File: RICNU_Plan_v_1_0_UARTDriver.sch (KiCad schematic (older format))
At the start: 7 parts, among them SW1 CL-SB-12B-01T, U3 SN74AHC126

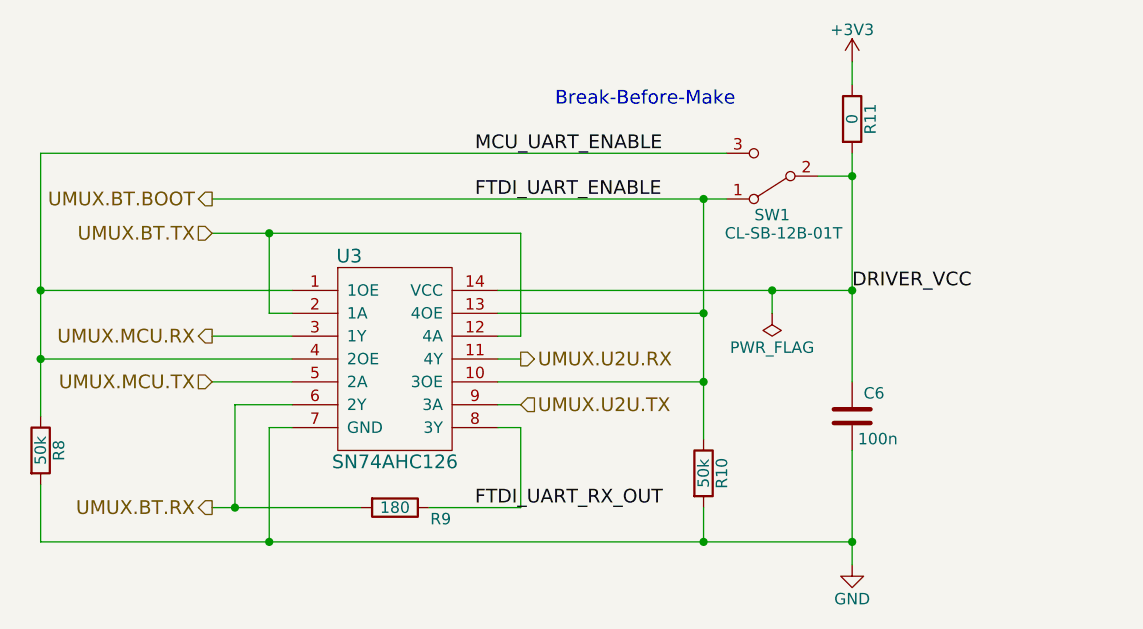
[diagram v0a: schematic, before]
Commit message: Re-routed CAN, RS-485, and debug connectors (wrong polarity in all)
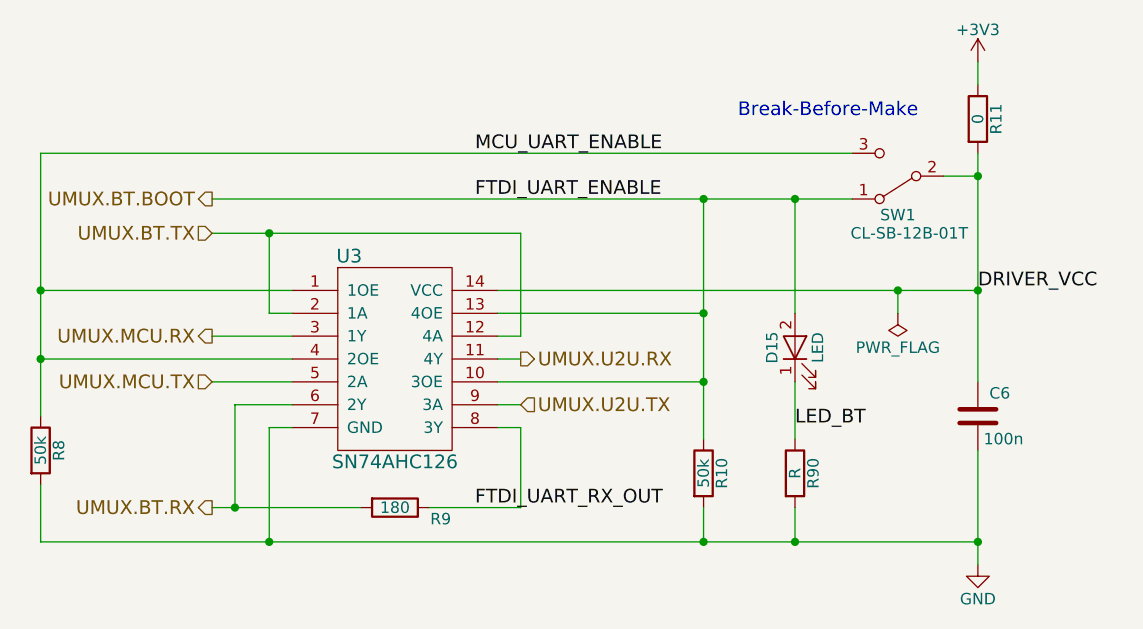
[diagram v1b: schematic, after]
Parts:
- added D15: LED, LEDs:LED_0402, symbol LED
- added R90: R, Resistors_SMD:R_0402_NoSilk, symbol R
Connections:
- net GND: now also R90.2
- net UMUX.BT.BOOT: now also D15.2 (A)
- new net LED_BT: D15.1 (K), R90.1
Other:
- moved on the sheet: C6, R11, SW1
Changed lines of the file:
@@
 L SW_SPDT SW1
 U 1 1 59E13A51
-P 7200 3300
-F 0 "SW1" H 7200 3470 50  0000 C CNN
-F 1 "CL-SB-12B-01T" H 7150 3550 50  0000 C CNN
-F 2 "RICNU_Plan_v_1_0:CL-SB-12B-01T" H 7200 3300 50  0001 C CNN
-F 3 "" H 7200 3300 50  0001 C CNN
-	1    7200 3300
+P 7750 3300
+F 0 "SW1" H 7750 3470 50  0000 C CNN
+F 1 "CL-SB-12B-01T" H 7700 3550 50  0000 C CNN
+F 2 "RICNU_Plan_v_1_0:CL-SB-12B-01T" H 7750 3300 50  0001 C CNN
+F 3 "" H 7750 3300 50  0001 C CNN
+	1    7750 3300
 	-1   0    0    1
 $EndComp
@@
 	6000 4000 6100 4000
 Wire Wire Line
-	6100 4000 6100 3550
-Wire Wire Line
-	6100 3550 4750 3550
+	6100 3550 6100 4000
+Wire Wire Line
+	4750 3550 6100 3550
 Wire Wire Line
 	4850 4750 4850 4300
@@
 Connection ~ 4000 3800
 Wire Wire Line
-	4750 3400 7000 3400
+	4750 3400 7550 3400
 Wire Wire Line
 	6900 3400 6900 4450
@@
 Connection ~ 4000 4100
 Wire Wire Line
-	4000 3200 7000 3200
+	4000 3200 7550 3200
 Connection ~ 6900 4200
 Connection ~ 6900 3900
@@
 L GND #PWR020
 U 1 1 59E69F5D
-P 7550 5000
-F 0 "#PWR020" H 7550 4750 50  0001 C CNN
-F 1 "GND" H 7550 4850 50  0000 C CNN
-F 2 "" H 7550 5000 50  0001 C CNN
-F 3 "" H 7550 5000 50  0001 C CNN
-	1    7550 5000
+P 8100 5000
+F 0 "#PWR020" H 8100 4750 50  0001 C CNN
+F 1 "GND" H 8100 4850 50  0000 C CNN
+F 2 "" H 8100 5000 50  0001 C CNN
+F 3 "" H 8100 5000 50  0001 C CNN
+	1    8100 5000
 	1    0    0    -1
 $EndComp
@@
 L +3V3 #PWR021
 U 1 1 59FDD411
-P 7550 2800
-F 0 "#PWR021" H 7550 2650 50  0001 C CNN
-F 1 "+3V3" H 7550 2940 50  0000 C CNN
-F 2 "" H 7550 2800 50  0001 C CNN
-F 3 "" H 7550 2800 50  0001 C CNN
-	1    7550 2800
+P 8100 2800
+F 0 "#PWR021" H 8100 2650 50  0001 C CNN
+F 1 "+3V3" H 8100 2940 50  0000 C CNN
+F 2 "" H 8100 2800 50  0001 C CNN
+F 3 "" H 8100 2800 50  0001 C CNN
+	1    8100 2800
 	1    0    0    -1
 $EndComp
@@
 L C C6
 U 1 1 59E69E0C
-P 7550 4350
-F 0 "C6" H 7600 4450 50  0000 L CNN
-F 1 "100n" H 7575 4250 50  0000 L CNN
-F 2 "Capacitors_SMD:C_0402_NoSilk" H 7588 4200 50  0001 C CNN
-F 3 "" H 7550 4350 50  0001 C CNN
-	1    7550 4350
-	1    0    0    -1
-$EndComp
-Wire Wire Line
-	7400 3300 7550 3300
-Connection ~ 7550 3800
-Wire Wire Line
-	7550 3200 7550 4200
-Wire Wire Line
-	7550 4500 7550 5000
-Wire Wire Line
-	6000 3800 7550 3800
-Wire Wire Line
-	4000 4900 7550 4900
-Connection ~ 7550 4900
+P 8100 4350
+F 0 "C6" H 8150 4450 50  0000 L CNN
+F 1 "100n" H 8125 4250 50  0000 L CNN
+F 2 "Capacitors_SMD:C_0402_NoSilk" H 8138 4200 50  0001 C CNN
+F 3 "" H 8100 4350 50  0001 C CNN
+	1    8100 4350
+	1    0    0    -1
+$EndComp
+Wire Wire Line
+	7950 3300 8100 3300
+Connection ~ 8100 3800
+Wire Wire Line
+	8100 3200 8100 4200
+Wire Wire Line
+	8100 4500 8100 5000
+Wire Wire Line
+	6000 3800 8100 3800
+Wire Wire Line
+	4000 4900 8100 4900
+Connection ~ 8100 4900
 Connection ~ 6900 4900
 Connection ~ 5000 4900
-Connection ~ 7550 3300
+Connection ~ 8100 3300
 Connection ~ 6900 3400
 Connection ~ 5000 3550
@@
 L R R11
 U 1 1 59F5E000
-P 7550 3050
-F 0 "R11" V 7630 3050 50  0000 C CNN
-F 1 "0" V 7550 3050 50  0000 C CNN
-F 2 "Resistors_SMD:R_0402_NoSilk" V 7480 3050 50  0001 C CNN
-F 3 "" H 7550 3050 50  0001 C CNN
-	1    7550 3050
-	1    0    0    -1
-$EndComp
-Wire Wire Line
-	7550 2800 7550 2900
-Text Notes 6250 3000 0    60   ~ 0
+P 8100 3050
+F 0 "R11" V 8180 3050 50  0000 C CNN
+F 1 "0" V 8100 3050 50  0000 C CNN
+F 2 "Resistors_SMD:R_0402_NoSilk" V 8030 3050 50  0001 C CNN
+F 3 "" H 8100 3050 50  0001 C CNN
+	1    8100 3050
+	1    0    0    -1
+$EndComp
+Wire Wire Line
+	8100 2800 8100 2900
+Text Notes 7050 3050 0    60   ~ 0
 Break-Before-Make
 $Comp
 L PWR_FLAG #FLG022
 U 1 1 59FD2D30
-P 7200 3900
-F 0 "#FLG022" H 7200 3975 50  0001 C CNN
-F 1 "PWR_FLAG" H 7200 4050 50  0000 C CNN
-F 2 "" H 7200 3900 50  0001 C CNN
-F 3 "" H 7200 3900 50  0001 C CNN
-	1    7200 3900
+P 7750 3900
+F 0 "#FLG022" H 7750 3975 50  0001 C CNN
+F 1 "PWR_FLAG" H 7750 4050 50  0000 C CNN
+F 2 "" H 7750 3900 50  0001 C CNN
+F 3 "" H 7750 3900 50  0001 C CNN
+	1    7750 3900
 	-1   0    0    1
 $EndComp
 Wire Wire Line
-	7200 3900 7200 3800
-Connection ~ 7200 3800
+	7750 3900 7750 3800
+Connection ~ 7750 3800
 Text Label 5900 3400 0    60   ~ 0
 FTDI_UART_ENABLE
@@
 Text Label 5900 4750 0    60   ~ 0
 FTDI_UART_RX_OUT
-Text Label 7550 3800 0    60   ~ 0
+Text Label 8100 3800 0    60   ~ 0
 DRIVER_VCC
+$Comp
+L LED D15
+U 1 1 5A2089D3
+P 7300 4050
+F 0 "D15" H 7300 4150 50  0000 C CNN
+F 1 "LED" H 7300 3950 50  0000 C CNN
+F 2 "LEDs:LED_0402" H 7300 4050 50  0001 C CNN
+F 3 "" H 7300 4050 50  0001 C CNN
+	1    7300 4050
+	0    -1   -1   0
+$EndComp
+$Comp
+L R R90
+U 1 1 5A208A32
+P 7300 4600
+F 0 "R90" V 7380 4600 50  0000 C CNN
+F 1 "R" V 7300 4600 50  0000 C CNN
+F 2 "Resistors_SMD:R_0402_NoSilk" V 7230 4600 50  0001 C CNN
+F 3 "" H 7300 4600 50  0001 C CNN
+	1    7300 4600
+	1    0    0    -1
+$EndComp
+Wire Wire Line
+	7300 4450 7300 4200
+Wire Wire Line
+	7300 4750 7300 4900
+Connection ~ 7300 4900
+Wire Wire Line
+	7300 3900 7300 3400
+Connection ~ 7300 3400
+Text Label 7300 4400 0    60   ~ 0
+LED_BT
 $EndSCHEMATC

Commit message: Added connections to monitor power, changed CANSTB MCU pin, moved LED pins around
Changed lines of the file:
@@
 	6000 4000 6100 4000
 Wire Wire Line
-	6100 3550 6100 4000
+	6100 4000 6100 3550
 Wire Wire Line
-	4750 3550 6100 3550
+	6100 3550 4750 3550
 Wire Wire Line
 	4850 4750 4850 4300

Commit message: Design freeze - ordered the board
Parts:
- D15: value LED -> LED_R
- R90: value R -> 660
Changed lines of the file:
@@
 P 7300 4050
 F 0 "D15" H 7300 4150 50  0000 C CNN
-F 1 "LED" H 7300 3950 50  0000 C CNN
+F 1 "LED_R" H 7300 3950 50  0000 C CNN
 F 2 "LEDs:LED_0402" H 7300 4050 50  0001 C CNN
 F 3 "" H 7300 4050 50  0001 C CNN
@@
 P 7300 4600
 F 0 "R90" V 7380 4600 50  0000 C CNN
-F 1 "R" V 7300 4600 50  0000 C CNN
+F 1 "660" V 7300 4600 50  0000 C CNN
 F 2 "Resistors_SMD:R_0402_NoSilk" V 7230 4600 50  0001 C CNN
 F 3 "" H 7300 4600 50  0001 C CNN

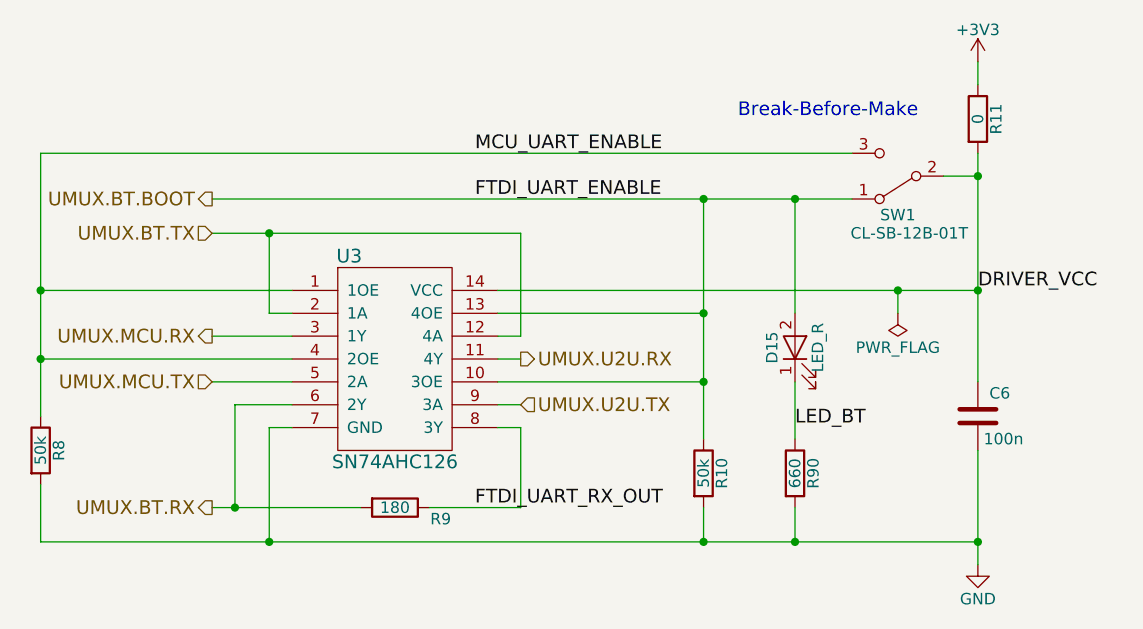
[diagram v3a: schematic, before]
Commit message: Various small changes like comment removal
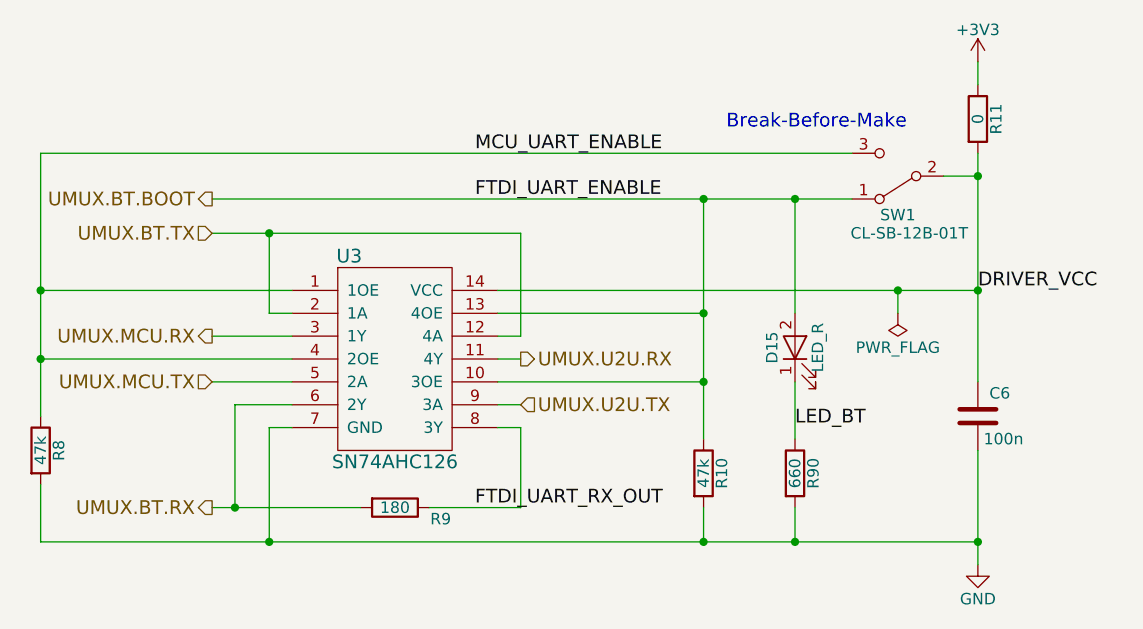
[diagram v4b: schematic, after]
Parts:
- R10, R8: value 50k -> 47k
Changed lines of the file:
@@
 P 4000 4500
 F 0 "R8" V 4080 4500 50  0000 C CNN
-F 1 "50k" V 4000 4500 50  0000 C CNN
+F 1 "47k" V 4000 4500 50  0000 C CNN
 F 2 "Resistors_SMD:R_0402_NoSilk" V 3930 4500 50  0001 C CNN
 F 3 "" H 4000 4500 50  0001 C CNN
@@
 P 6900 4600
 F 0 "R10" V 6980 4600 50  0000 C CNN
-F 1 "50k" V 6900 4600 50  0000 C CNN
+F 1 "47k" V 6900 4600 50  0000 C CNN
 F 2 "Resistors_SMD:R_0402_NoSilk" V 6830 4600 50  0001 C CNN
 F 3 "" H 6900 4600 50  0001 C CNN
@@
 Wire Wire Line
 	8100 2800 8100 2900
-Text Notes 7050 3050 0    60   ~ 0
+Text Notes 7000 3100 0    60   ~ 0
 Break-Before-Make
 $Comp
